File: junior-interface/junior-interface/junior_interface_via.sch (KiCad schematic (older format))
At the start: 27 parts, among them IC1 6522, IC13 74LS27, IC14 74LS01, IC15 74LS30, IC16 74LS00, J11 Conn_01x20_Male, J13 +12V, J14 -5V, J15 -12V, J16 0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

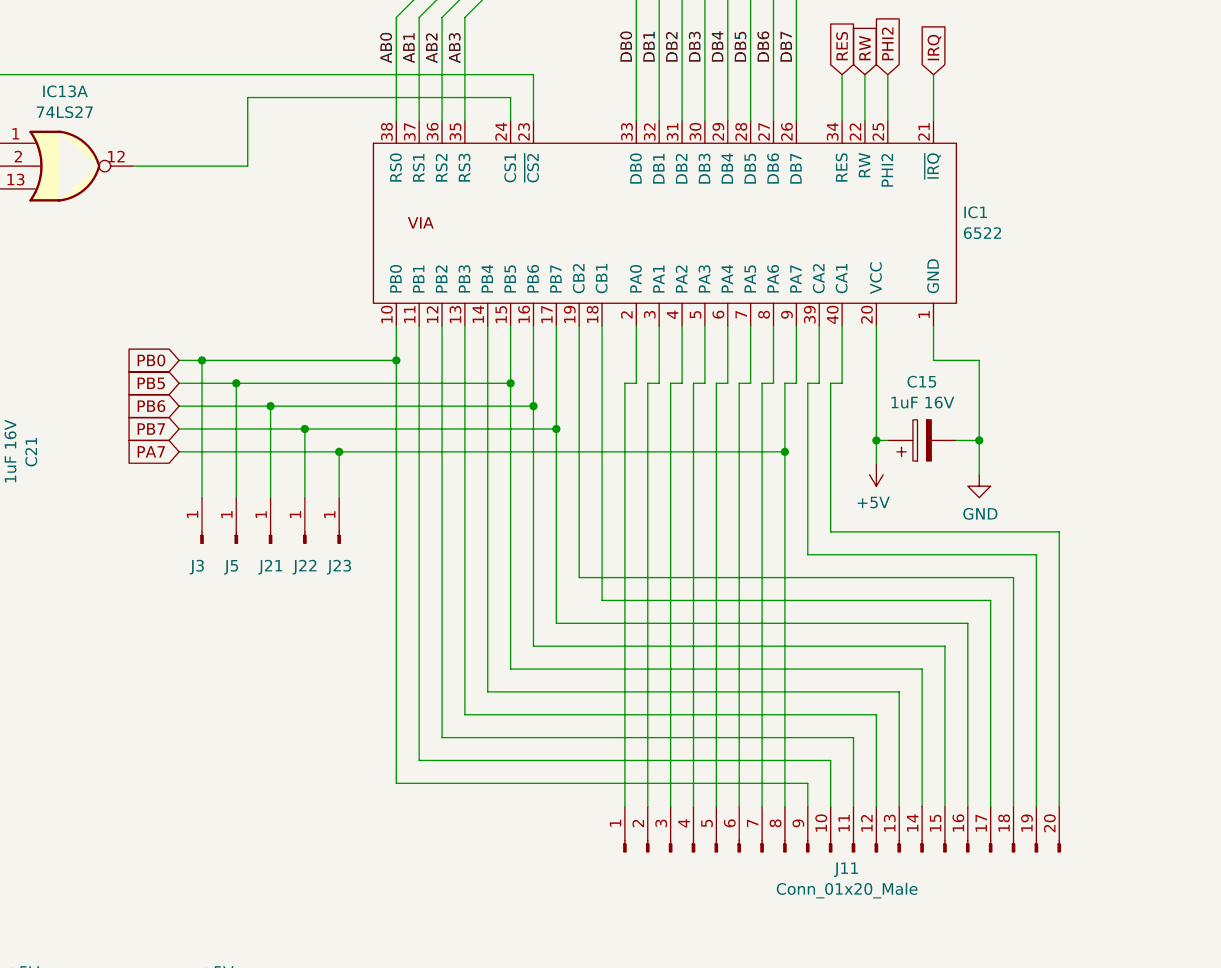
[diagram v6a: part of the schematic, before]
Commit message: junior interface routage complet
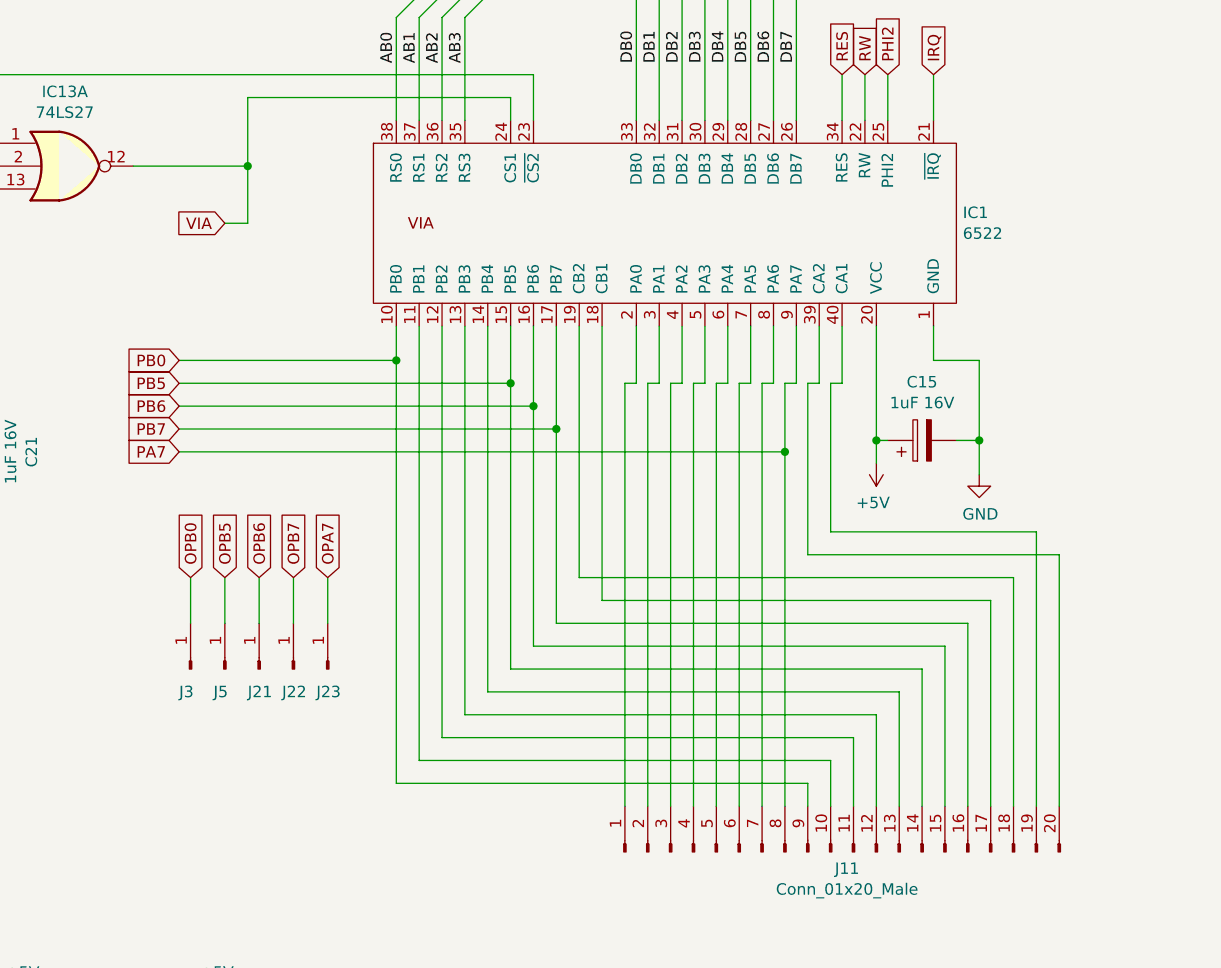
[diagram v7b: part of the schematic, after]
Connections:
- net PA7: no longer J23.1 (Pin_1)
- net PB0: no longer J3.1 (Pin_1)
- net PB5: no longer J5.1 (Pin_1)
- net PB6: no longer J21.1 (Pin_1)
- net PB7: no longer J22.1 (Pin_1)
- net VIA: now reaches IC1.24 (CS1), IC13.12
- net at J11.19 (Pin_19): now also IC1.40 (CA1); no longer IC1.39 (CA2)
- net at J11.20 (Pin_20): now also IC1.39 (CA2); no longer IC1.40 (CA1)
- new net OPA7: J23.1 (Pin_1)
- new net OPB0: J3.1 (Pin_1)
- new net OPB5: J5.1 (Pin_1)
- new net OPB6: J21.1 (Pin_1)
- new net OPB7: J22.1 (Pin_1)
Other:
- moved on the sheet: J21, J22, J23, J3, J5
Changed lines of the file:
@@
 	6150 3200 6150 3950
-Wire Wire Line
-	6150 3950 7150 3950
-Wire Wire Line
-	7150 3950 7150 5050
 Wire Wire Line
 	6450 3450 6450 3550
@@
 Wire Wire Line
 	6250 3200 6250 3850
-Wire Wire Line
-	6250 3850 7250 3850
-Wire Wire Line
-	7250 3850 7250 5050
 Wire Wire Line
 	6050 3500 6050 5050
@@
 Text GLabel 3400 3100 0    50   Input ~ 0
 PB0
-Wire Wire Line
-	3400 3100 3500 3100
-Wire Wire Line
-	3400 3200 3650 3200
-Wire Wire Line
-	3400 3300 3800 3300
-Wire Wire Line
-	3400 3400 3950 3400
-Wire Wire Line
-	3400 3500 4100 3500
 $Comp
 L Connector:Conn_01x01_Male J3
 U 1 1 5FC98A7A
-P 3500 3900
-F 0 "J3" V 3400 3950 50  0000 R CNN
-F 1 " " V 3563 3812 50  0000 R CNN
-F 2 "elektor:PIN" H 3500 3900 50  0001 C CNN
-F 3 "~" H 3500 3900 50  0001 C CNN
-	1    3500 3900
+P 3450 4450
+F 0 "J3" V 3350 4500 50  0000 R CNN
+F 1 " " V 3513 4362 50  0000 R CNN
+F 2 "elektor:PIN" H 3450 4450 50  0001 C CNN
+F 3 "~" H 3450 4450 50  0001 C CNN
+	1    3450 4450
 	0    -1   -1   0
 $EndComp
@@
 L Connector:Conn_01x01_Male J5
 U 1 1 5FCA1379
-P 3650 3900
-F 0 "J5" V 3550 3950 50  0000 R CNN
-F 1 " " V 3713 3812 50  0000 R CNN
-F 2 "elektor:PIN" H 3650 3900 50  0001 C CNN
-F 3 "~" H 3650 3900 50  0001 C CNN
-	1    3650 3900
+P 3600 4450
+F 0 "J5" V 3500 4500 50  0000 R CNN
+F 1 " " V 3663 4362 50  0000 R CNN
+F 2 "elektor:PIN" H 3600 4450 50  0001 C CNN
+F 3 "~" H 3600 4450 50  0001 C CNN
+	1    3600 4450
 	0    -1   -1   0
 $EndComp
@@
 L Connector:Conn_01x01_Male J21
 U 1 1 5FCA7A65
-P 3800 3900
-F 0 "J21" V 3700 3950 50  0000 R CNN
-F 1 " " V 3863 3812 50  0000 R CNN
-F 2 "elektor:PIN" H 3800 3900 50  0001 C CNN
-F 3 "~" H 3800 3900 50  0001 C CNN
-	1    3800 3900
+P 3750 4450
+F 0 "J21" V 3650 4500 50  0000 R CNN
+F 1 " " V 3813 4362 50  0000 R CNN
+F 2 "elektor:PIN" H 3750 4450 50  0001 C CNN
+F 3 "~" H 3750 4450 50  0001 C CNN
+	1    3750 4450
 	0    -1   -1   0
 $EndComp
@@
 L Connector:Conn_01x01_Male J22
 U 1 1 5FCAE0E4
-P 3950 3900
-F 0 "J22" V 3850 3950 50  0000 R CNN
-F 1 " " V 4013 3812 50  0000 R CNN
-F 2 "elektor:PIN" H 3950 3900 50  0001 C CNN
-F 3 "~" H 3950 3900 50  0001 C CNN
-	1    3950 3900
+P 3900 4450
+F 0 "J22" V 3800 4500 50  0000 R CNN
+F 1 " " V 3963 4362 50  0000 R CNN
+F 2 "elektor:PIN" H 3900 4450 50  0001 C CNN
+F 3 "~" H 3900 4450 50  0001 C CNN
+	1    3900 4450
 	0    -1   -1   0
 $EndComp
@@
 L Connector:Conn_01x01_Male J23
 U 1 1 5FCB47B1
-P 4100 3900
-F 0 "J23" V 4000 3950 50  0000 R CNN
-F 1 " " V 4163 3812 50  0000 R CNN
-F 2 "elektor:PIN" H 4100 3900 50  0001 C CNN
-F 3 "~" H 4100 3900 50  0001 C CNN
-	1    4100 3900
-	0    -1   -1   0
-$EndComp
-Wire Wire Line
-	3500 3700 3500 3100
-Connection ~ 3500 3100
-Wire Wire Line
-	3500 3100 4350 3100
-Wire Wire Line
-	3650 3700 3650 3200
-Connection ~ 3650 3200
-Wire Wire Line
-	3650 3200 4850 3200
-Wire Wire Line
-	3800 3700 3800 3300
-Connection ~ 3800 3300
-Wire Wire Line
-	4100 3700 4100 3500
-Connection ~ 4100 3500
-Wire Wire Line
-	4100 3500 6050 3500
-Wire Wire Line
-	3800 3300 4950 3300
-Wire Wire Line
-	3950 3700 3950 3400
-Connection ~ 3950 3400
-Wire Wire Line
-	3950 3400 5050 3400
+P 4050 4450
+F 0 "J23" V 3950 4500 50  0000 R CNN
+F 1 " " V 4113 4362 50  0000 R CNN
+F 2 "elektor:PIN" H 4050 4450 50  0001 C CNN
+F 3 "~" H 4050 4450 50  0001 C CNN
+	1    4050 4450
+	0    -1   -1   0
+$EndComp
 $Comp
 L power:GND #PWR0198
@@
 	1    0    0    -1
 $EndComp
+Text GLabel 3600 2500 0    50   Input ~ 0
+VIA
+Wire Wire Line
+	3600 2500 3700 2500
+Wire Wire Line
+	3700 2500 3700 2250
+Connection ~ 3700 2250
+Wire Wire Line
+	7250 3950 7250 5050
+Wire Wire Line
+	6150 3950 7250 3950
+Wire Wire Line
+	6250 3850 7150 3850
+Wire Wire Line
+	7150 3850 7150 5050
+Wire Wire Line
+	3400 3100 4350 3100
+Wire Wire Line
+	3400 3200 4850 3200
+Wire Wire Line
+	3400 3300 4950 3300
+Wire Wire Line
+	3400 3400 5050 3400
+Wire Wire Line
+	3400 3500 6050 3500
+Text GLabel 3450 4050 1    50   Input ~ 0
+OPB0
+Text GLabel 3600 4050 1    50   Input ~ 0
+OPB5
+Text GLabel 3750 4050 1    50   Input ~ 0
+OPB6
+Text GLabel 3900 4050 1    50   Input ~ 0
+OPB7
+Text GLabel 4050 4050 1    50   Input ~ 0
+OPA7
+Wire Wire Line
+	3450 4050 3450 4250
+Wire Wire Line
+	3600 4050 3600 4250
+Wire Wire Line
+	3750 4050 3750 4250
+Wire Wire Line
+	3900 4050 3900 4250
+Wire Wire Line
+	4050 4050 4050 4250
 Wire Bus Line
 	1650 1500 8150 1500

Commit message: junior interface update
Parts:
- IC1: symbol junior_computer:6522 -> junior-interface-rescue:6522-junior_computer
- renumbered J3 to J40
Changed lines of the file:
@@
 EESchema Schematic File Version 4
-LIBS:junior-interface-cache
 EELAYER 30 0
 EELAYER END
@@
 	4550 1600 4650 1500
 $Comp
-L junior_computer:6522 IC1
+L junior-interface-rescue:6522-junior_computer IC1
 U 1 1 6010E98F
 P 5200 2500
@@
 PB0
 $Comp
-L Connector:Conn_01x01_Male J3
+L Connector:Conn_01x01_Male J40
 U 1 1 5FC98A7A
 P 3450 4450
-F 0 "J3" V 3350 4500 50  0000 R CNN
+F 0 "J40" V 3350 4500 50  0000 R CNN
 F 1 " " V 3513 4362 50  0000 R CNN
 F 2 "elektor:PIN" H 3450 4450 50  0001 C CNN
